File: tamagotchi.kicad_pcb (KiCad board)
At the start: 2 copper layers, 60.8 x 77.1 mm, 9 parts, among them SW1 SW_Push, SW2 SW_Push, SW3 SW_Push, U1 XIAO-ESP32-C3-SMD, U2 HS96L03W2C03

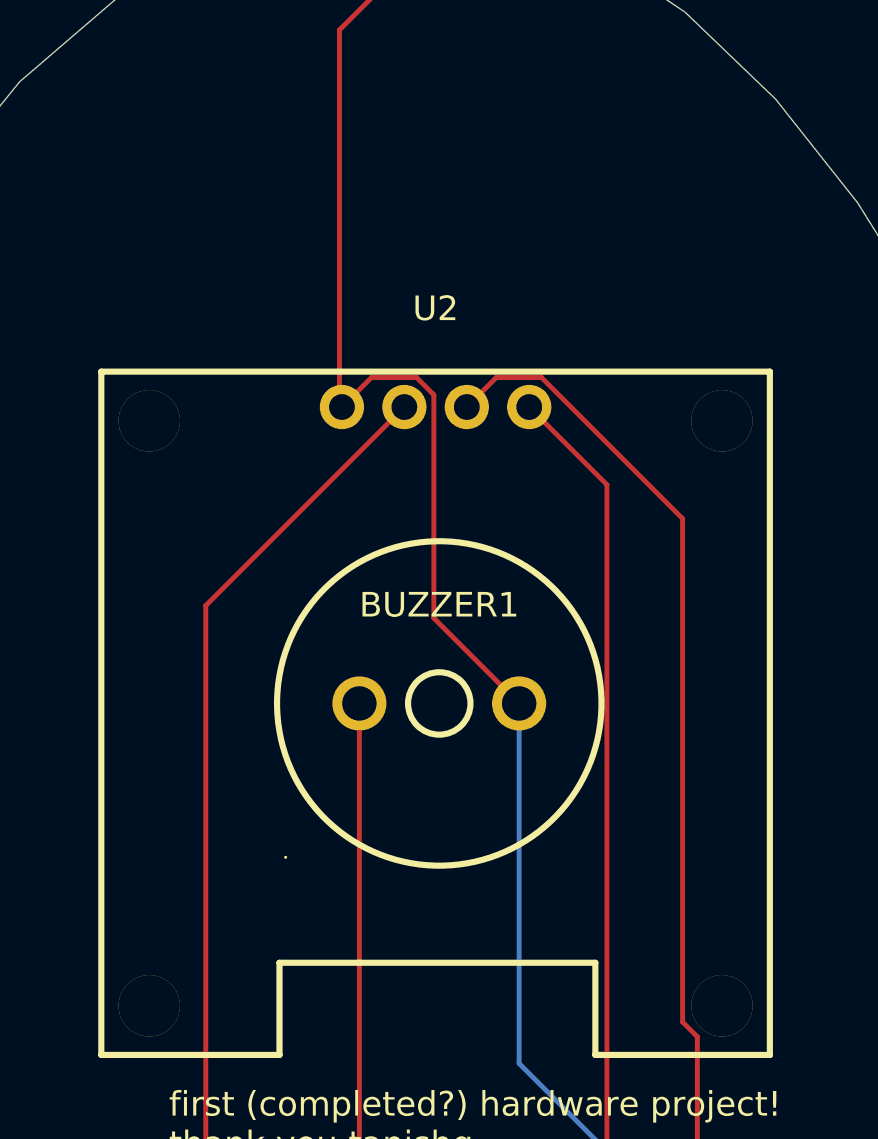
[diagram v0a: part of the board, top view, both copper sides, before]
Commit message: redid some routing and added a furby design because i keep thinking of matt rose furbies when i see tamagotchi
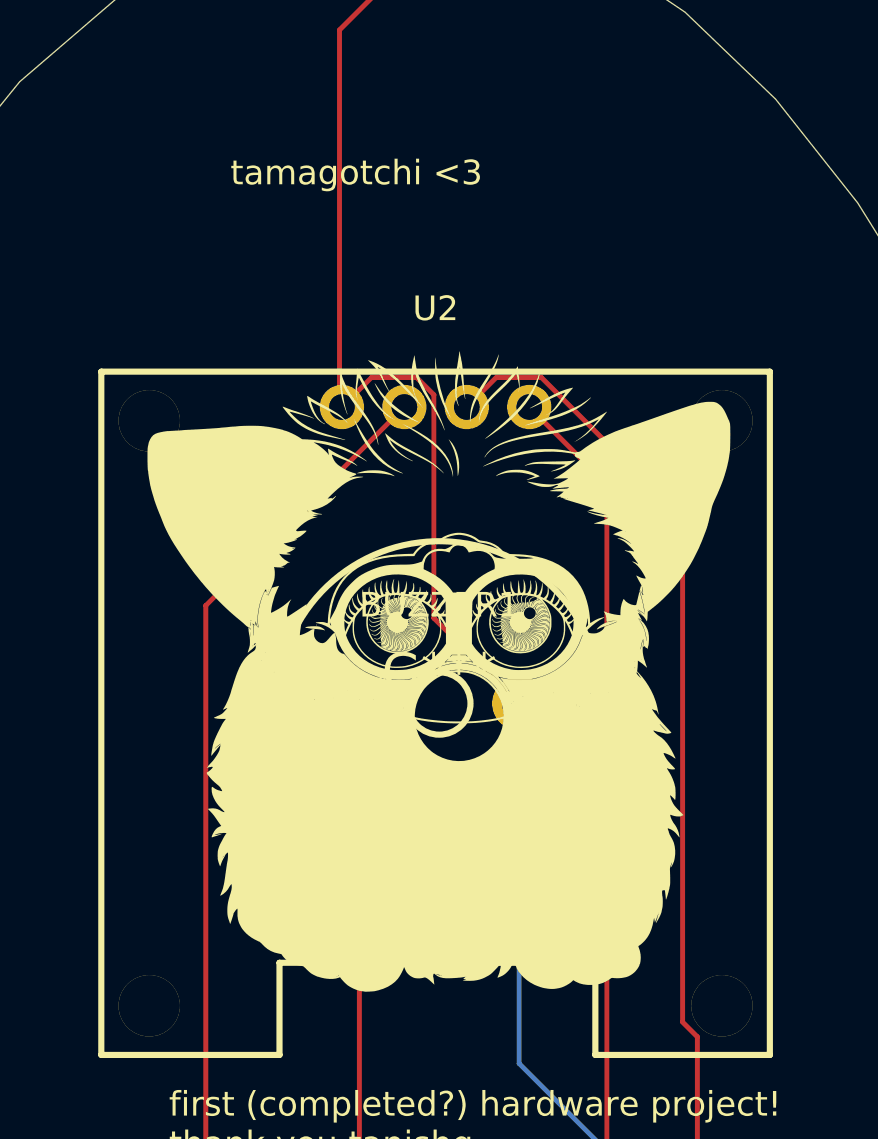
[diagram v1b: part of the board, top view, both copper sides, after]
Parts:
- added G***: LOGO, LOGO, F.Cu at (72.0, 71.2)
